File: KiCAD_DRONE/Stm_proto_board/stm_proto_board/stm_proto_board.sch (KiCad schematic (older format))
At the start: 3 parts, among them J1 Conn_01x32, J2 Conn_01x32, U1 STM32F103R(C-D-E)Tx

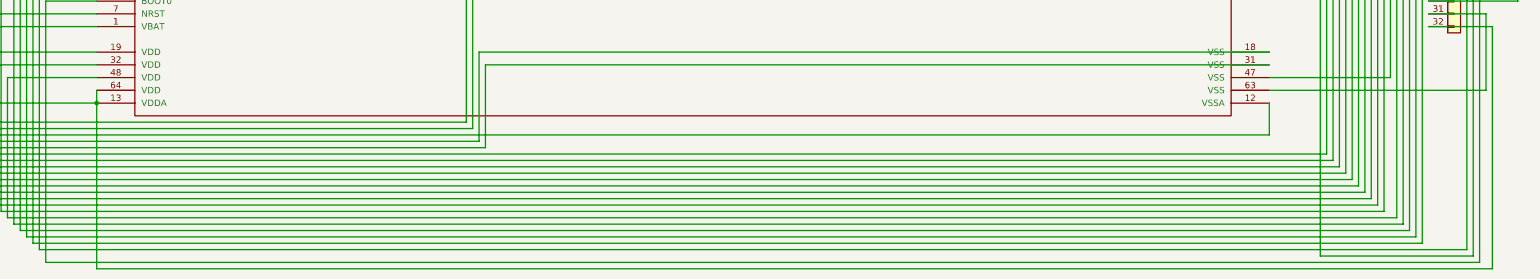
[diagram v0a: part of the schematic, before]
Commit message: added the m60 files for the stm proto board and the gate driver IC. updated code to drive motor. not sure if it works or not.
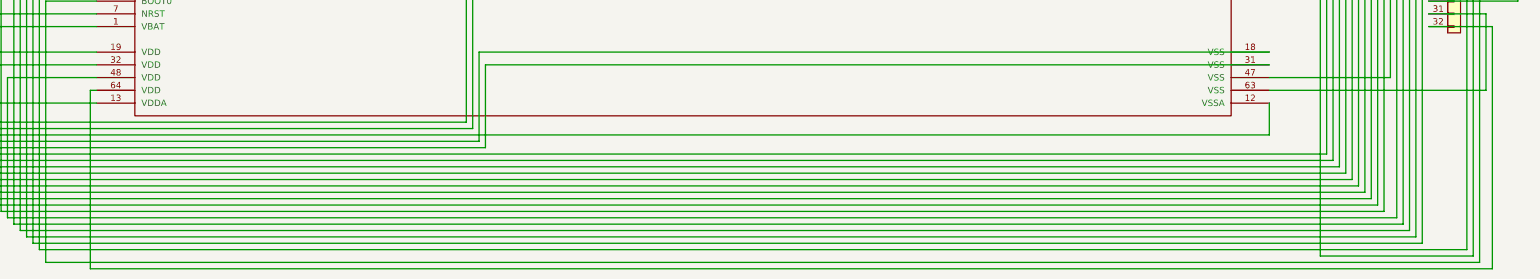
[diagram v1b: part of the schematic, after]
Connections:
- net at J1.20 (Pin_20), U1.13 (VDDA): no longer J2.32 (Pin_32), U1.64 (VDD)
- new net: J2.32 (Pin_32), U1.64 (VDD)
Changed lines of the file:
@@
 	14700 6350 14250 6350
-Wire Wire Line
-	3800 6950 3800 7050
-Wire Wire Line
-	3800 8350 14750 8350
 Wire Wire Line
 	14750 8350 14750 6450
 Wire Wire Line
 	14750 6450 14250 6450
-Connection ~ 3800 7050
 Wire Wire Line
-	3800 7050 3800 8350
+	3800 6950 3750 6950
+Wire Wire Line
+	3750 6950 3750 8350
+Wire Wire Line
+	3750 8350 14750 8350
 $EndSCHEMATC
